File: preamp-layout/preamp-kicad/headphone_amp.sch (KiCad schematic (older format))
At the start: 23 parts, among them J72 Conn_01x04_Male, J73 Conn_01x03_Male, J74 Conn_01x03_Male, J75 Conn_01x03_Male, J76 Conn_01x03_Female, J77 Conn_01x04_Female, U20 TPA6120

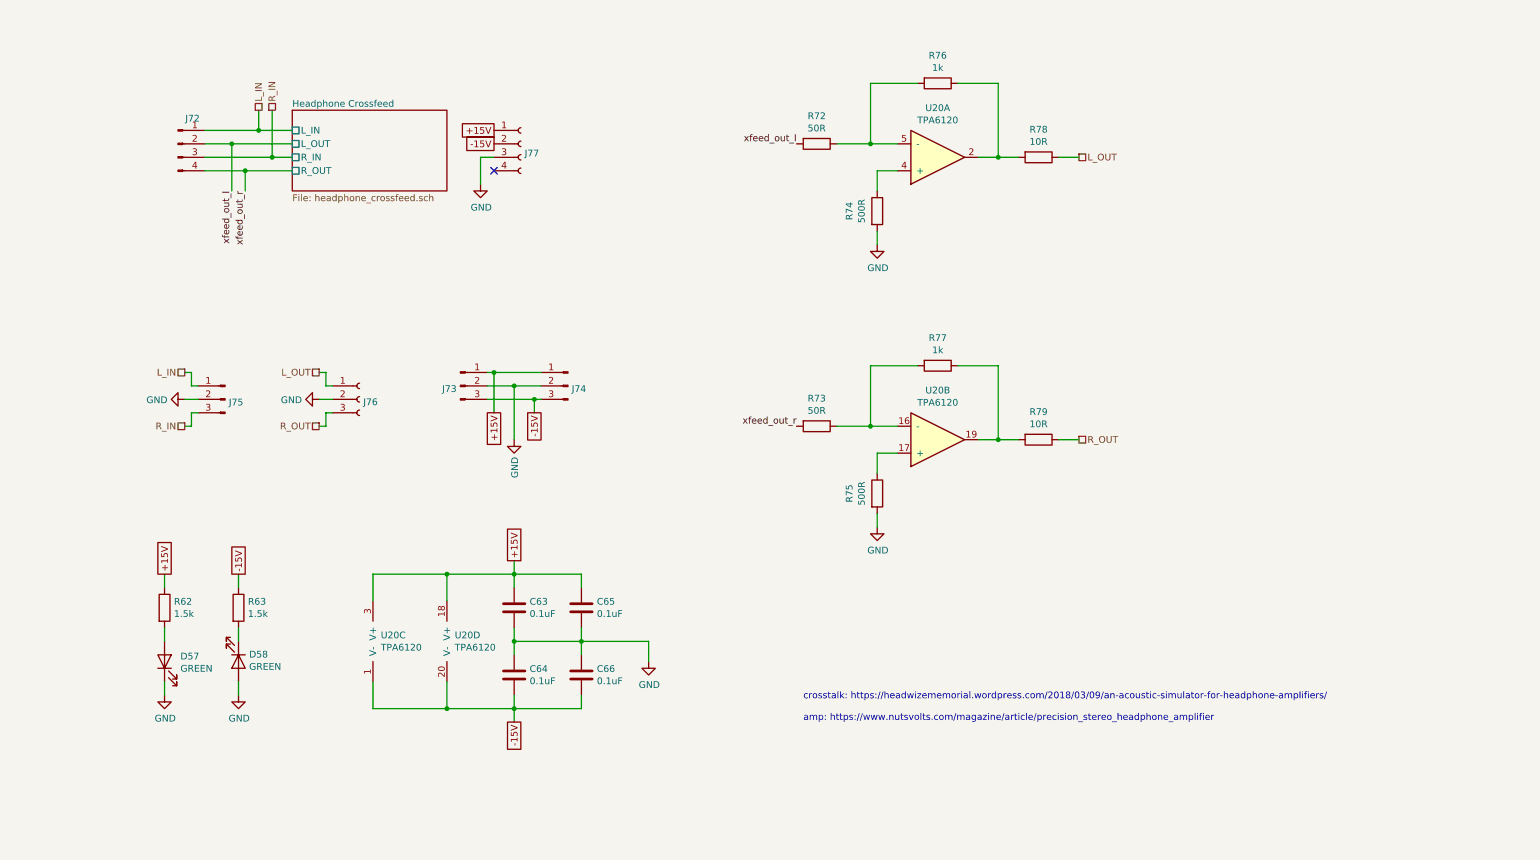
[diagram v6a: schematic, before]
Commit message: Conn / Pin Updates
Updated cable headers, pin names, MCU conn layout. MCP4902 changeout for custom symbol.
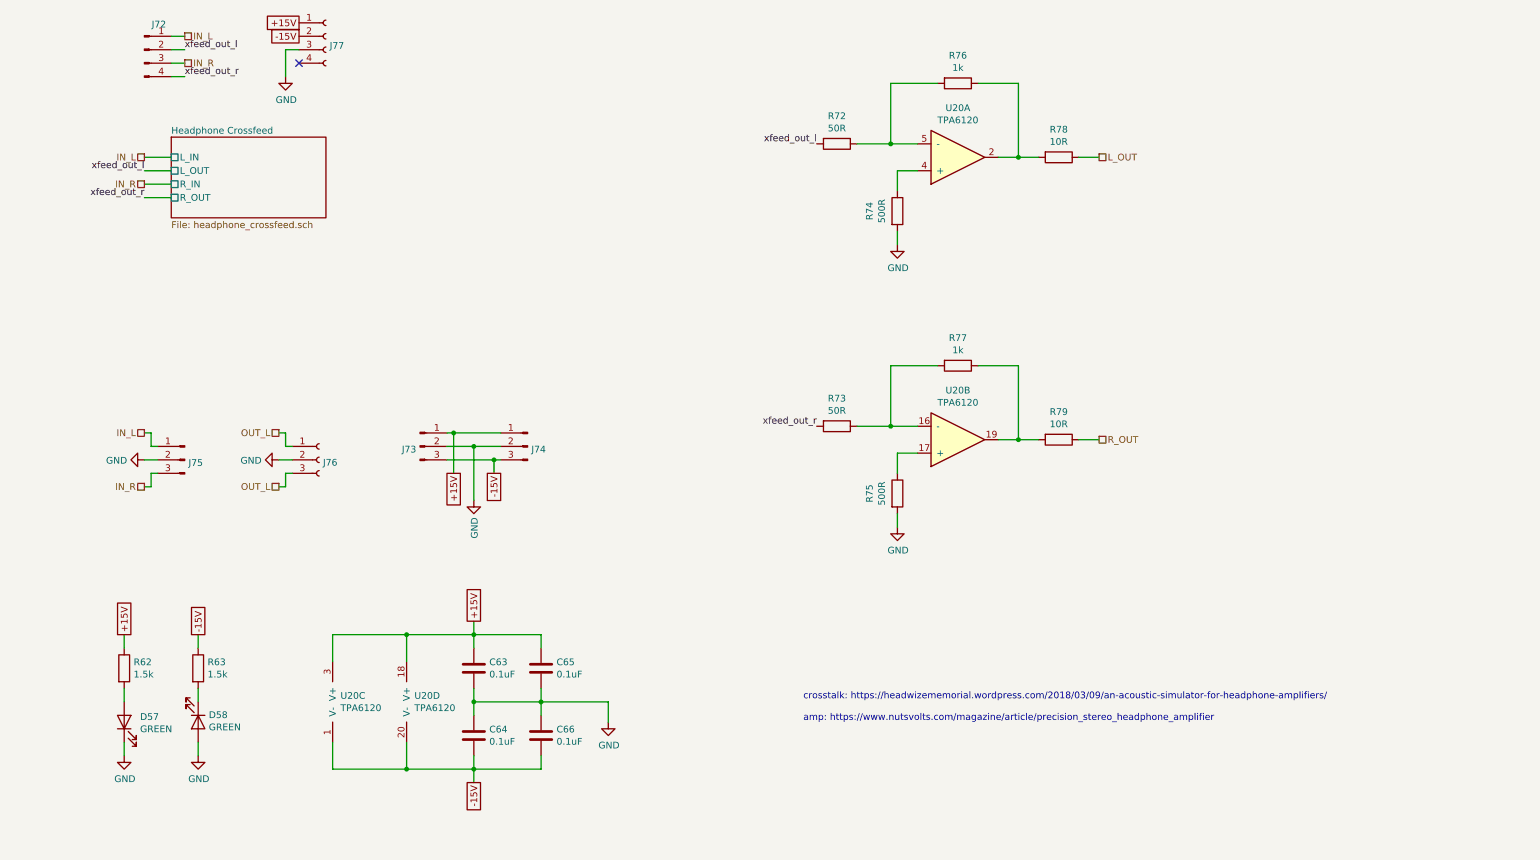
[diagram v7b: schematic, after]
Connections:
- net L_OUT: no longer J76.1 (Pin_1)
- net R_OUT: no longer J76.3 (Pin_3)
- net L_IN renamed IN_L
- net R_IN renamed IN_R
- new net OUT_L: J76.1 (Pin_1), J76.3 (Pin_3)
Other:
- moved on the sheet: C63, C64, C65, C66, D57, D58, J72, J73, J74, J75, J76, J77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

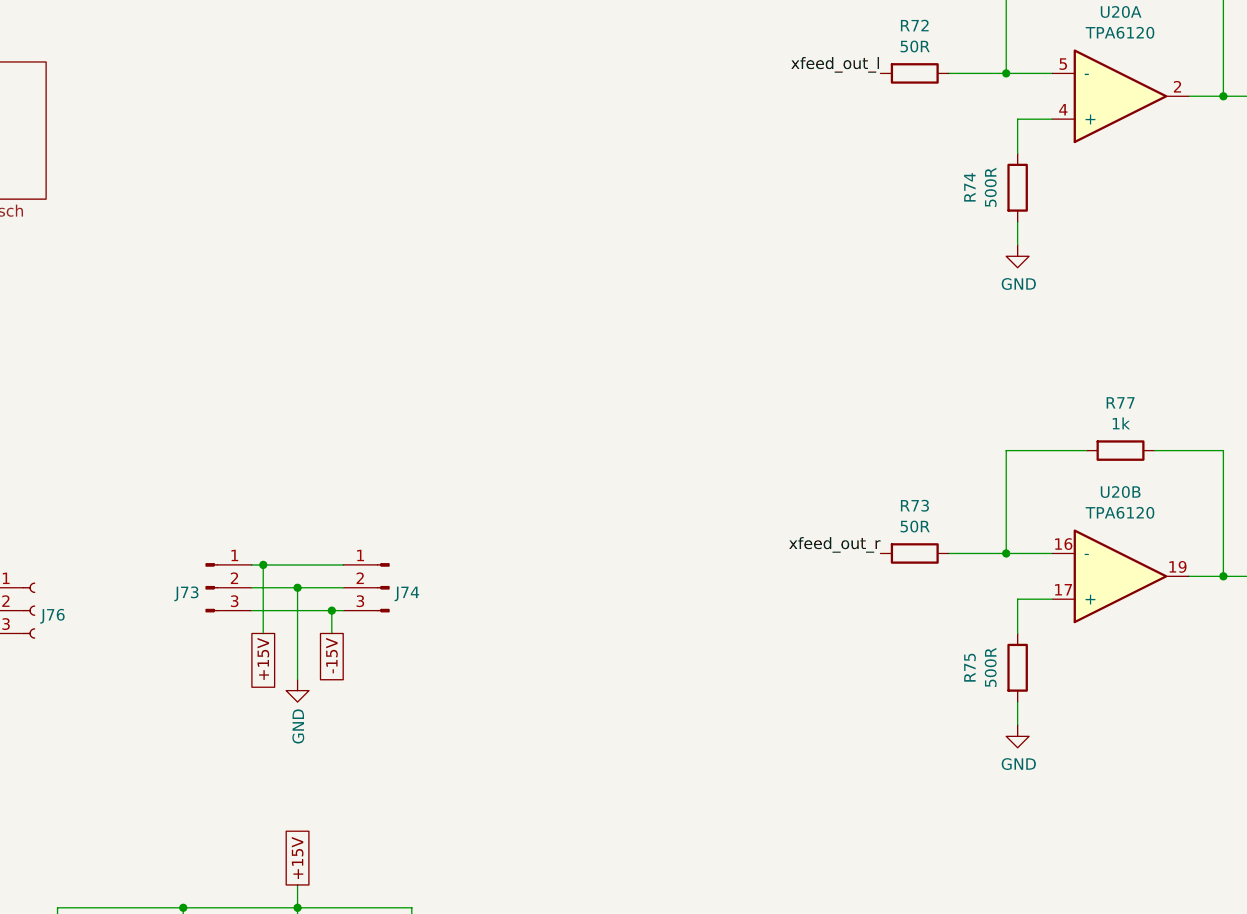
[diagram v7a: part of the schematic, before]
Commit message: Power Supply Update
Grounding made more clear, tied to chassis on AC board. Pins renamed. Aligned with AC wall power convention. General cleanup.
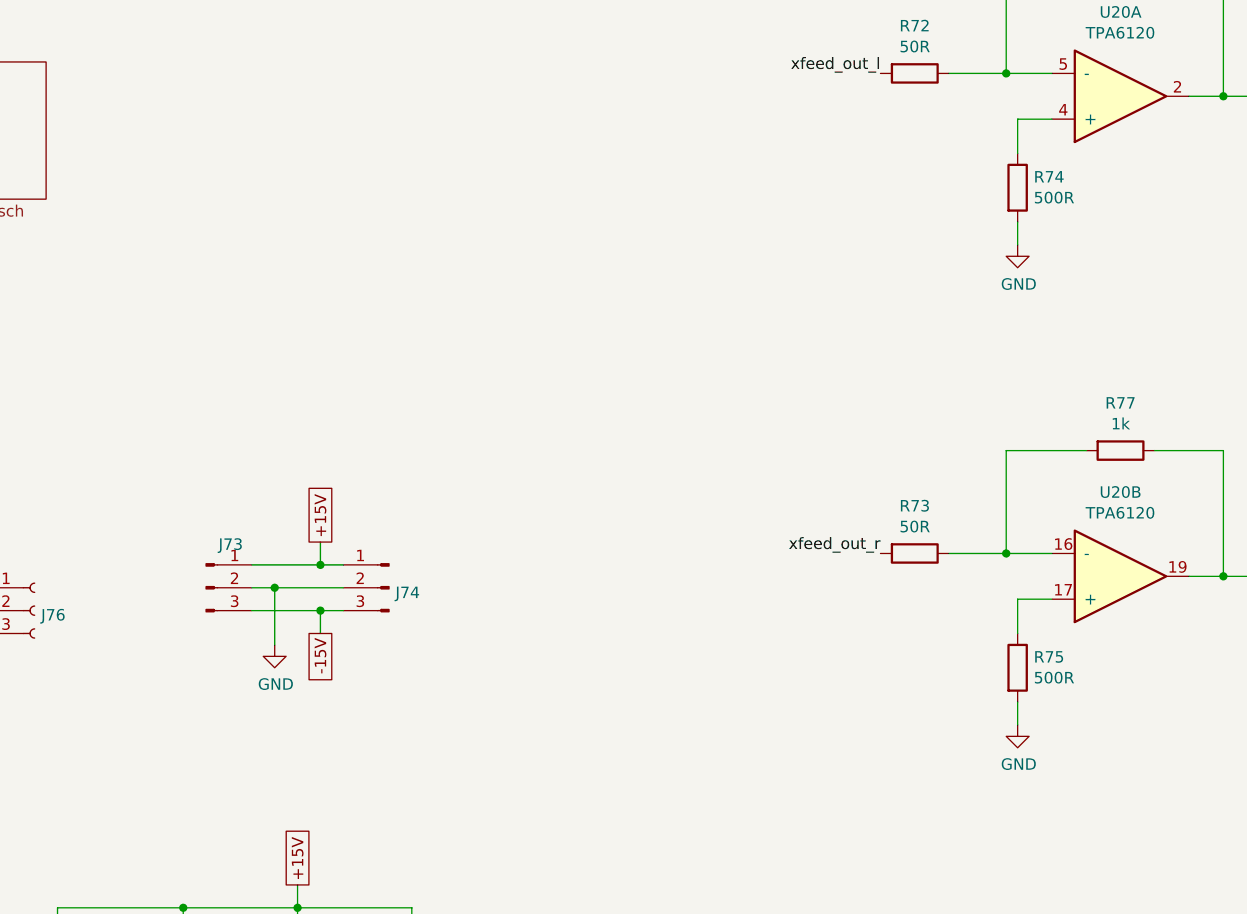
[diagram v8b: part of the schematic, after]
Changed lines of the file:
@@
 AR Path="/5E80BFEC/5F1C3374" Ref="R?"  Part="1"
 AR Path="/5E4A803E/5F1C3374" Ref="R74"  Part="1"
-F 0 "R74" V 7443 2650 50  0000 C CNN
-F 1 "500R" V 7534 2650 50  0000 C CNN
+F 0 "R74" H 7720 2696 50  0000 L CNN
+F 1 "500R" H 7720 2605 50  0000 L CNN
 F 2 "Resistor_SMD:R_1206_3216Metric_Pad1.42x1.75mm_HandSolder" V 7580 2650 50  0001 C CNN
 F 3 "~" H 7650 2650 50  0001 C CNN
@@
 AR Path="/5E80BFEC/5F1D9CED" Ref="R?"  Part="1"
 AR Path="/5E4A803E/5F1D9CED" Ref="R75"  Part="1"
-F 0 "R75" V 7443 4750 50  0000 C CNN
-F 1 "500R" V 7534 4750 50  0000 C CNN
+F 0 "R75" H 7720 4796 50  0000 L CNN
+F 1 "500R" H 7720 4705 50  0000 L CNN
 F 2 "Resistor_SMD:R_1206_3216Metric_Pad1.42x1.75mm_HandSolder" V 7580 4750 50  0001 C CNN
 F 3 "~" H 7650 4750 50  0001 C CNN
@@
 AR Path="/6009D432/647A3EBE" Ref="J?"  Part="1"
 AR Path="/5E4A803E/647A3EBE" Ref="J73"  Part="1"
-F 0 "J73" H 4072 4378 50  0000 R CNN
+F 0 "J73" H 4208 4589 50  0000 C CNN
 F 1 "Conn_01x03_Male" H 4072 4333 50  0001 R CNN
 F 2 "Connector_JST:JST_EH_B3B-EH-A_1x03_P2.50mm_Vertical" H 4100 4400 50  0001 C CNN
@@
 Wire Wire Line
 	3200 1450 3100 1450
-Text GLabel 4350 4600 3    50   UnSpc ~ 0
+Text GLabel 4600 4200 1    50   UnSpc ~ 0
 +15V
-Text GLabel 4650 4600 3    50   UnSpc ~ 0
+Text GLabel 4600 4600 3    50   UnSpc ~ 0
 -15V
 $Comp
 L power:GND #PWR?
 U 1 1 601F478F
-P 4500 4800
+P 4400 4650
 AR Path="/6009D432/601F478F" Ref="#PWR?"  Part="1"
 AR Path="/5E4A803E/601F478F" Ref="#PWR0106"  Part="1"
-F 0 "#PWR0106" H 4500 4550 50  0001 C CNN
-F 1 "GND" V 4505 4672 50  0000 R CNN
-F 2 "" H 4500 4800 50  0001 C CNN
-F 3 "" H 4500 4800 50  0001 C CNN
-	1    4500 4800
-	1    0    0    -1
-$EndComp
-Wire Wire Line
-	4300 4300 4350 4300
-Wire Wire Line
-	4300 4400 4500 4400
-Wire Wire Line
-	4300 4500 4650 4500
-Wire Wire Line
-	4350 4600 4350 4300
-Connection ~ 4350 4300
-Wire Wire Line
-	4350 4300 4700 4300
-Wire Wire Line
-	4650 4600 4650 4500
-Connection ~ 4650 4500
-Wire Wire Line
-	4650 4500 4700 4500
-Wire Wire Line
-	4500 4800 4500 4400
-Connection ~ 4500 4400
-Wire Wire Line
-	4500 4400 4700 4400
+F 0 "#PWR0106" H 4400 4400 50  0001 C CNN
+F 1 "GND" H 4405 4477 50  0000 C CNN
+F 2 "" H 4400 4650 50  0001 C CNN
+F 3 "" H 4400 4650 50  0001 C CNN
+	1    4400 4650
+	1    0    0    -1
+$EndComp
+Wire Wire Line
+	4300 4500 4600 4500
+Wire Wire Line
+	4600 4600 4600 4500
 Wire Wire Line
 	4500 6800 4000 6800
@@
 Wire Wire Line
 	2050 2550 2250 2550
+Wire Wire Line
+	4300 4300 4600 4300
+Wire Wire Line
+	4300 4400 4400 4400
+Wire Wire Line
+	4400 4650 4400 4400
+Connection ~ 4400 4400
+Connection ~ 4600 4500
+Wire Wire Line
+	4600 4500 4700 4500
+Wire Wire Line
+	4400 4400 4700 4400
+Wire Wire Line
+	4600 4200 4600 4300
+Connection ~ 4600 4300
+Wire Wire Line
+	4600 4300 4700 4300
 $EndSCHEMATC
